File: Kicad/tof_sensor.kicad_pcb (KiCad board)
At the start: 2 copper layers, 86.4 x 45.7 mm, 52 parts, among them J1 Conn_01x06_Male, J2 Conn_01x05, Q1 BSH202,215, SW1 SW_DIP_x03, U1 MIC5504-2.8YM5, U2 PIC24FJ64GA002, U3 VL53L0X, U4 VL53L0X, U5 PCA9306

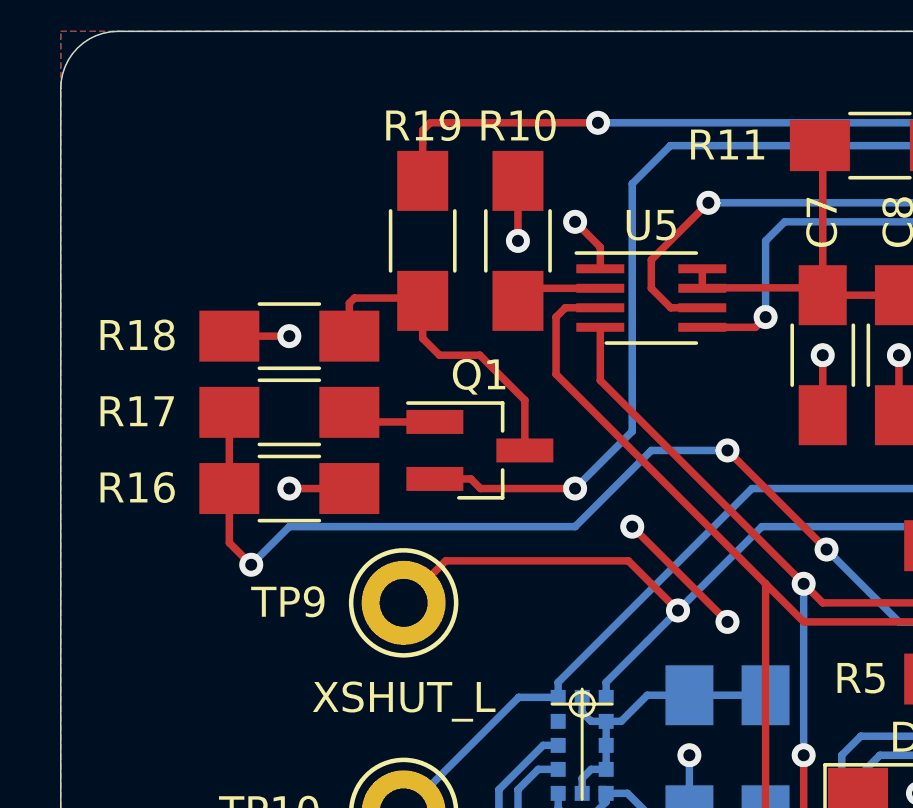
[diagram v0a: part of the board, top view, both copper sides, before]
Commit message: Changed P-MOS by N-MOS for int circuit.
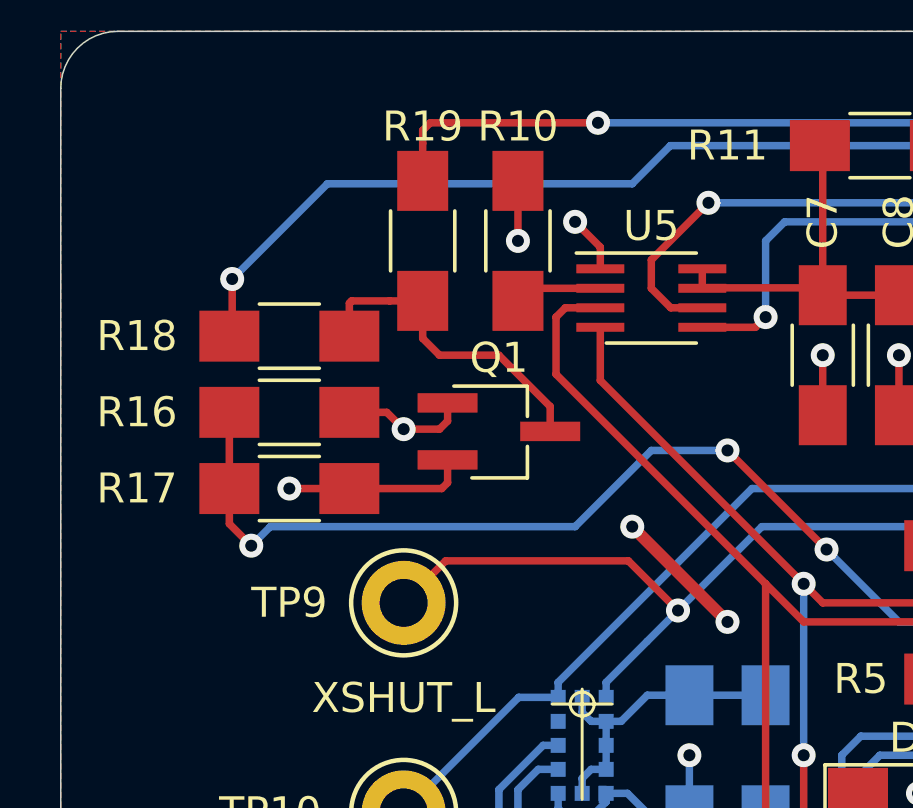
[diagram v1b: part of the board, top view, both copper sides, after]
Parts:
- Q1: value BSH202,215 -> Q_NMOS_SGD; footprint TO_SOT_Packages_SMD:SOT-23_Handsoldering -> TO_SOT_Packages_SMD:TSOT-23_HandSoldering
- moved R16 2.54 mm to (118.7, 73.7)
- moved R17 2.54 mm to (118.7, 76.2)
- moved Q1 0.90 mm to (125.7, 74.3)
- turned R18 to 180 degrees
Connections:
- Q1 pad 1: Net-(Q1-Pad1) -> GND
- Q1 pad 2: VCC -> Net-(Q1-Pad2)
- R17 pad 2: Net-(Q1-Pad1) -> Net-(Q1-Pad2)
- R18 pad 1: GND -> Net-(Q1-Pad3)
- R18 pad 2: Net-(Q1-Pad3) -> VCC
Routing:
- net Net-(Q1-Pad2): track 0.00 -> 6.12 mm, vias 0 -> 1
- net Net-(Q1-Pad1): track 3.62 -> 0.00 mm
- net GND: track 72.4 -> 73.6 mm, vias 23 -> 22
- net /INT_OUT_VDD: track 52.6 -> 51.7 mm
- net VCC: track 85.5 -> 86.4 mm
- net Net-(Q1-Pad3): track 11.4 -> 12.1 mm

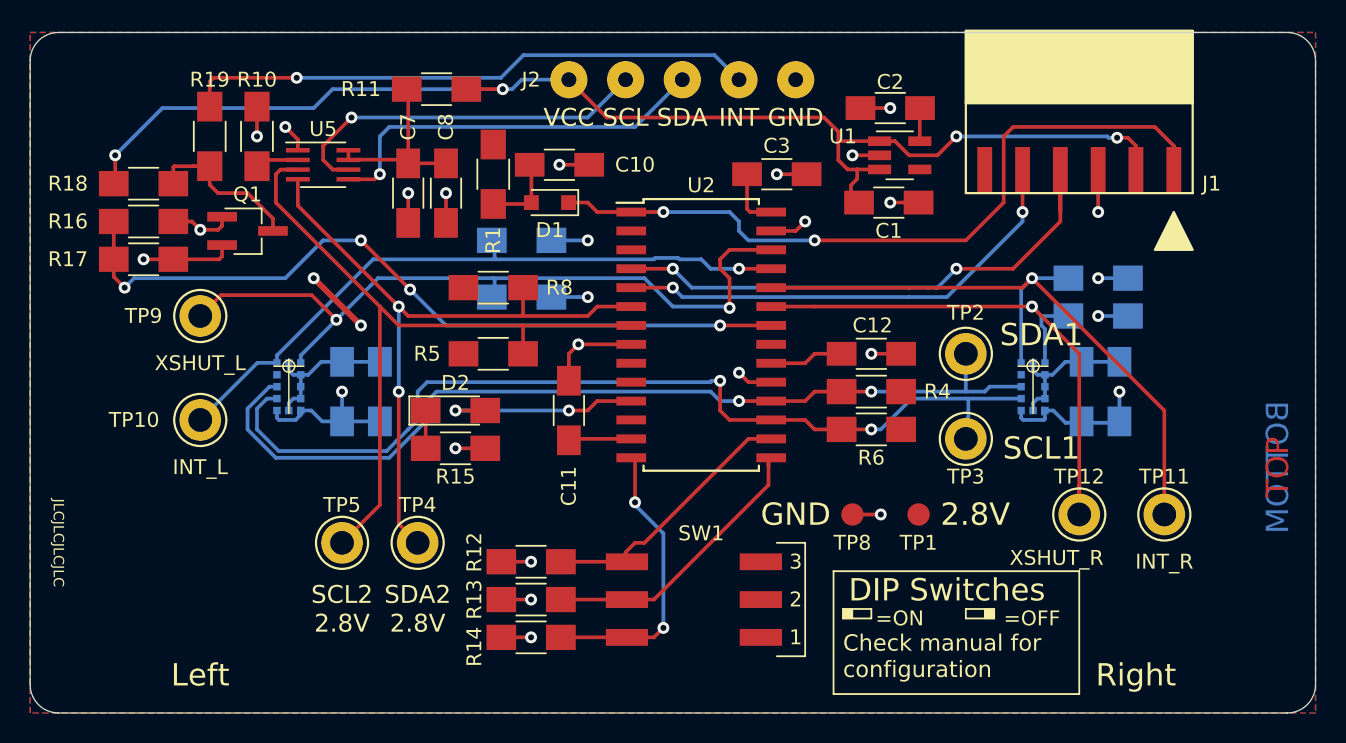
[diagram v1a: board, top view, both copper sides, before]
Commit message: Updated testpoints
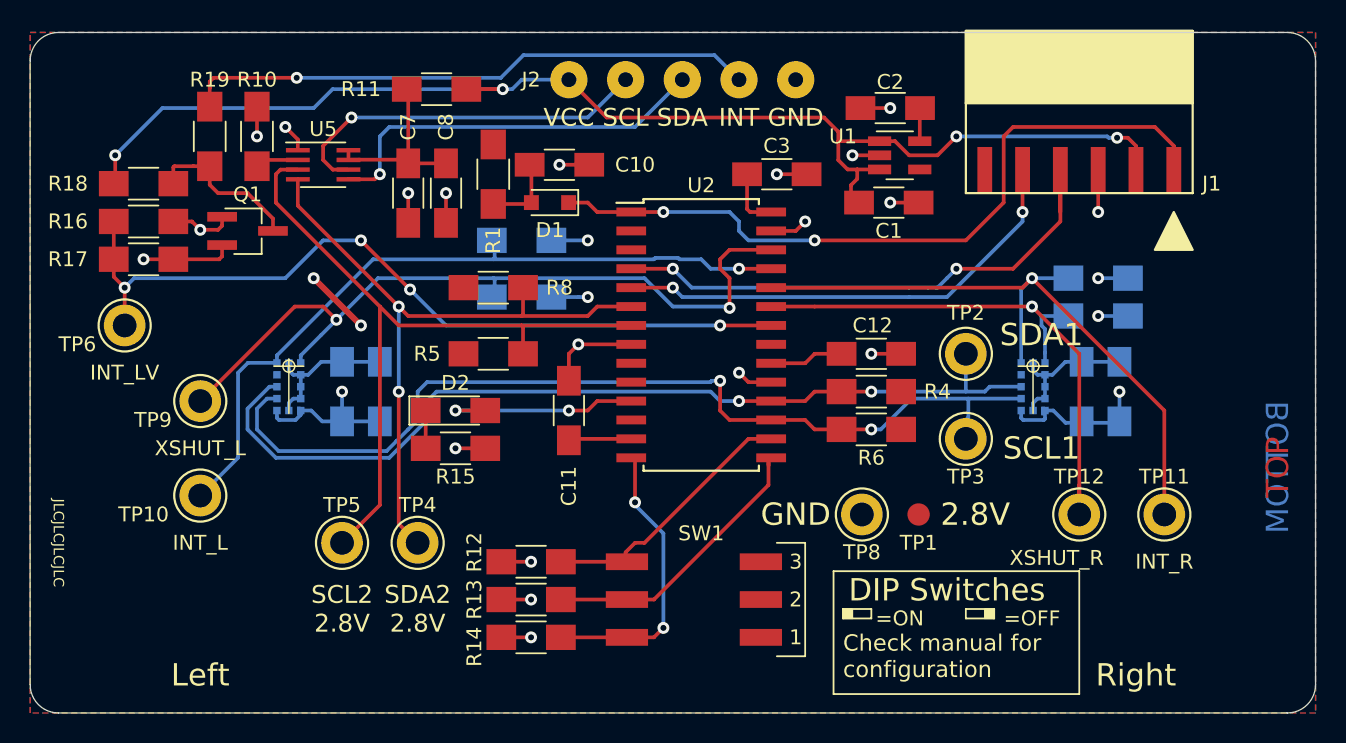
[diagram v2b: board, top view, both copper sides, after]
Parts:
- added TP6: TestPoint_Probe, Measurement_Points:Test_Point_Keystone_5010-5014_Multipurpose, F.Cu at (117.5, 80.6)
- TP8: footprint Measurement_Points:Measurement_Point_Round-SMD-Pad_Small -> Measurement_Points:Test_Point_Keystone_5010-5014_Multipurpose
- moved TP9 5.71 mm to (122.6, 85.7)
- moved TP10 5.08 mm to (122.6, 92.1)
- moved TP8 0.63 mm to (167.0, 93.3)
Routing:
- net /INT_L: track 44.6 -> 50.0 mm
- net /INT_OUT_VDD: track 51.7 -> 54.2 mm
- net GND: track 73.6 -> 71.7 mm, vias 22 -> 21
- net /XSHUT_L: track 51.0 -> 52.8 mm
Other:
- board text added: "INT_LV"
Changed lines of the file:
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@@
   (general
     (thickness 1.6)
-    (drawings 68)
+    (drawings 69)
     (tracks 438)
     (zones 0)
-    (modules 52)
+    (modules 53)
     (nets 39)
   )
@@
     (uvia_drill 0.1)
   )
+  (module Measurement_Points:Test_Point_Keystone_5010-5014_Multipurpose (layer F.Cu)
+    (at 167.005 93.345)
+    (descr "Keystone Miniature THM Test Point 5010-5014, http://www.keyelco.com/product-pdf.cfm?p=1319")
+    (tags "Through Hole Mount Test Points")
+    (attr virtual)
+    (fp_text reference TP8 (at 0 2.54) (layer F.SilkS)
+      (effects (font (size 1 1) (thickness 0.15)))
+    )
+    (fp_text value TestPoint_Probe (at 0 2.75) (layer F.Fab)
+      (effects (font (size 1 1) (thickness 0.15)))
+    )
+    (fp_circle (center 0 0) (end 2 0) (layer F.CrtYd) (width 0.05))
+    (fp_line (start -1.25 -0.4) (end 1.25 -0.4) (layer F.Fab) (width 0.15))
+    (fp_line (start 1.25 -0.4) (end 1.25 0.4) (layer F.Fab) (width 0.15))
+    (fp_line (start 1.25 0.4) (end -1.25 0.4) (layer F.Fab) (width 0.15))
+    (fp_line (start -1.25 0.4) (end -1.25 -0.4) (layer F.Fab) (width 0.15))
+    (fp_circle (center 0 0) (end 1.6 0) (layer F.Fab) (width 0.15))
+    (fp_circle (center 0 0) (end 1.75 0) (layer F.SilkS) (width 0.15))
+    (pad 1 thru_hole circle (at 0 0) (size 2.8 2.8) (drill 1.6) (layers *.Cu *.Mask)
+      (net 2 GND))
+  )
+  (module Measurement_Points:Test_Point_Keystone_5010-5014_Multipurpose (layer F.Cu)
+    (at 117.475 80.645)
+    (descr "Keystone Miniature THM Test Point 5010-5014, http://www.keyelco.com/product-pdf.cfm?p=1319")
+    (tags "Through Hole Mount Test Points")
+    (attr virtual)
+    (fp_text reference TP6 (at -3.175 1.27) (layer F.SilkS)
+      (effects (font (size 1 1) (thickness 0.15)))
+    )
+    (fp_text value TestPoint_Probe (at 0 2.75) (layer F.Fab)
+      (effects (font (size 1 1) (thickness 0.15)))
+    )
+    (fp_circle (center 0 0) (end 2 0) (layer F.CrtYd) (width 0.05))
+    (fp_line (start -1.25 -0.4) (end 1.25 -0.4) (layer F.Fab) (width 0.15))
+    (fp_line (start 1.25 -0.4) (end 1.25 0.4) (layer F.Fab) (width 0.15))
+    (fp_line (start 1.25 0.4) (end -1.25 0.4) (layer F.Fab) (width 0.15))
+    (fp_line (start -1.25 0.4) (end -1.25 -0.4) (layer F.Fab) (width 0.15))
+    (fp_circle (center 0 0) (end 1.6 0) (layer F.Fab) (width 0.15))
+    (fp_circle (center 0 0) (end 1.75 0) (layer F.SilkS) (width 0.15))
+    (pad 1 thru_hole circle (at 0 0) (size 2.8 2.8) (drill 1.6) (layers *.Cu *.Mask)
+      (net 37 /INT_OUT_VDD))
+  )
   (module TO_SOT_Packages_SMD:TSOT-23_HandSoldering (layer F.Cu)
     (at 125.73 74.295)
@@
   )
   (module Measurement_Points:Test_Point_Keystone_5010-5014_Multipurpose (layer F.Cu)
-    (at 122.555 80.01)
+    (at 122.555 85.725)
     (descr "Keystone Miniature THM Test Point 5010-5014, http://www.keyelco.com/product-pdf.cfm?p=1319")
     (tags "Through Hole Mount Test Points")
     (attr virtual)
-    (fp_text reference TP9 (at -3.81 0) (layer F.SilkS)
+    (fp_text reference TP9 (at -3.175 1.27) (layer F.SilkS)
       (effects (font (size 1 1) (thickness 0.15)))
     )
@@
   )
   (module Measurement_Points:Test_Point_Keystone_5010-5014_Multipurpose (layer F.Cu)
-    (at 122.555 86.995)
+    (at 122.555 92.075)
     (descr "Keystone Miniature THM Test Point 5010-5014, http://www.keyelco.com/product-pdf.cfm?p=1319")
     (tags "Through Hole Mount Test Points")
     (attr virtual)
-    (fp_text reference TP10 (at -4.445 0) (layer F.SilkS)
+    (fp_text reference TP10 (at -3.81 1.27) (layer F.SilkS)
       (effects (font (size 1 1) (thickness 0.15)))
     )
@@
       (rotate (xyz 0 0 0))
     )
-  )
-  (module Measurement_Points:Measurement_Point_Round-SMD-Pad_Small (layer F.Cu)
-    (at 166.37 93.345)
-    (descr "Mesurement Point, Round, SMD Pad, DM 1.5mm,")
-    (tags "Mesurement Point Round SMD Pad 1.5mm")
-    (attr virtual)
-    (fp_text reference TP8 (at 0 1.905) (layer F.SilkS)
-      (effects (font (size 1 1) (thickness 0.15)))
-    )
-    (fp_text value TestPoint_Probe (at 0 2) (layer F.Fab)
-      (effects (font (size 1 1) (thickness 0.15)))
-    )
-    (fp_circle (center 0 0) (end 1 0) (layer F.CrtYd) (width 0.05))
-    (pad 1 smd circle (at 0 0) (size 1.5 1.5) (layers F.Cu F.Mask)
-      (net 2 GND))
   )
   (module Measurement_Points:Measurement_Point_Round-SMD-Pad_Small (layer F.Cu)
@@
     )
   )
-  (gr_text INT_L (at 122.555 90.17) (layer F.SilkS)
+  (gr_text INT_LV (at 117.475 83.82) (layer F.SilkS)
+    (effects (font (size 1 1) (thickness 0.25)))
+  )
+  (gr_text INT_L (at 122.555 95.25) (layer F.SilkS)
     (effects (font (size 1 1) (thickness 0.25)))
   )
@@
     (effects (font (size 1.5 1.5) (thickness 0.3)))
   )
-  (gr_text XSHUT_L (at 122.555 83.185) (layer F.SilkS)
+  (gr_text XSHUT_L (at 122.555 88.9) (layer F.SilkS)
     (effects (font (size 1 1) (thickness 0.25)))
   )
@@
   (segment (start 148.685 69.85) (end 146.685 69.85) (width 0.25) (layer F.Cu) (net 2) (status 10))
   (via (at 146.685 69.85) (size 0.8) (drill 0.4) (layers F.Cu B.Cu) (net 2))
-  (segment (start 166.37 93.345) (end 168.275 93.345) (width 0.25) (layer F.Cu) (net 2) (status 10))
-  (via (at 168.275 93.345) (size 0.8) (drill 0.4) (layers F.Cu B.Cu) (net 2))
   (via (at 139.7 88.9) (size 0.8) (drill 0.4) (layers F.Cu B.Cu) (net 2))
   (segment (start 141.7 88.9) (end 139.7 88.9) (width 0.25) (layer F.Cu) (net 2) (status 10))
@@
   (segment (start 142.24 76.2) (end 142.335 76.105) (width 0.25) (layer B.Cu) (net 13))
   (segment (start 134.165 76.2) (end 142.24 76.2) (width 0.25) (layer B.Cu) (net 13))
-  (segment (start 126.39 83.16) (end 127.705 83.16) (width 0.25) (layer B.Cu) (net 13))
-  (segment (start 122.555 86.995) (end 126.39 83.16) (width 0.25) (layer B.Cu) (net 13))
   (segment (start 129.305 83.16) (end 129.305 82.66) (width 0.25) (layer B.Cu) (net 14) (status 10))
   (via (at 158.115 79.465) (size 0.8) (drill 0.4) (layers F.Cu B.Cu) (net 14))
@@
   (segment (start 134.495 77.47) (end 142.24 77.47) (width 0.25) (layer B.Cu) (net 14))
   (via (at 131.7 80.265) (size 0.8) (drill 0.4) (layers F.Cu B.Cu) (net 14))
-  (segment (start 130.81 79.375) (end 131.7 80.265) (width 0.25) (layer F.Cu) (net 14))
   (segment (start 134.495 77.47) (end 131.7 80.265) (width 0.25) (layer B.Cu) (net 14))
   (segment (start 131.7 80.265) (end 130.6675 81.2975) (width 0.25) (layer B.Cu) (net 14))
-  (segment (start 130.045001 78.610001) (end 130.81 79.375) (width 0.25) (layer F.Cu) (net 14))
-  (segment (start 123.954999 78.610001) (end 130.045001 78.610001) (width 0.25) (layer F.Cu) (net 14))
-  (segment (start 122.555 80.01) (end 123.954999 78.610001) (width 0.25) (layer F.Cu) (net 14))
   (segment (start 142.24 77.47) (end 152.4 77.47) (width 0.25) (layer B.Cu) (net 14))
   (segment (start 158.025 79.375) (end 154.305 79.375) (width 0.25) (layer B.Cu) (net 14))
@@
   (segment (start 124.02 73.95) (end 124.02 73.345) (width 0.25) (layer F.Cu) (net 2))
   (segment (start 123.75 74.22) (end 124.02 73.95) (width 0.25) (layer F.Cu) (net 2))
+  (segment (start 125.095 89.535) (end 122.555 92.075) (width 0.25) (layer B.Cu) (net 13))
+  (segment (start 125.095 83.82) (end 125.095 89.535) (width 0.25) (layer B.Cu) (net 13))
+  (segment (start 127.705 83.16) (end 125.755 83.16) (width 0.25) (layer B.Cu) (net 13))
+  (segment (start 125.755 83.16) (end 125.095 83.82) (width 0.25) (layer B.Cu) (net 13))
+  (segment (start 131.7 80.265) (end 130.81 79.375) (width 0.25) (layer F.Cu) (net 14))
+  (segment (start 128.905 79.375) (end 122.555 85.725) (width 0.25) (layer F.Cu) (net 14))
+  (segment (start 130.81 79.375) (end 128.905 79.375) (width 0.25) (layer F.Cu) (net 14))
   (segment (start 123.19 69.945) (end 122.65 69.945) (width 0.25) (layer F.Cu) (net 36))
   (segment (start 122.65 69.945) (end 122.555 69.85) (width 0.25) (layer F.Cu) (net 36))
@@
   (segment (start 116.745 77.375) (end 116.745 76.2) (width 0.25) (layer F.Cu) (net 37))
   (segment (start 117.475 78.105) (end 116.745 77.375) (width 0.25) (layer F.Cu) (net 37))
+  (segment (start 117.475 78.105) (end 117.475 80.645) (width 0.25) (layer F.Cu) (net 37))
   (segment (start 124.02 76.005) (end 124.02 75.245) (width 0.25) (layer F.Cu) (net 38))
   (segment (start 120.745 76.2) (end 123.825 76.2) (width 0.25) (layer F.Cu) (net 38))

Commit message: Replaced mounting holes that went missing
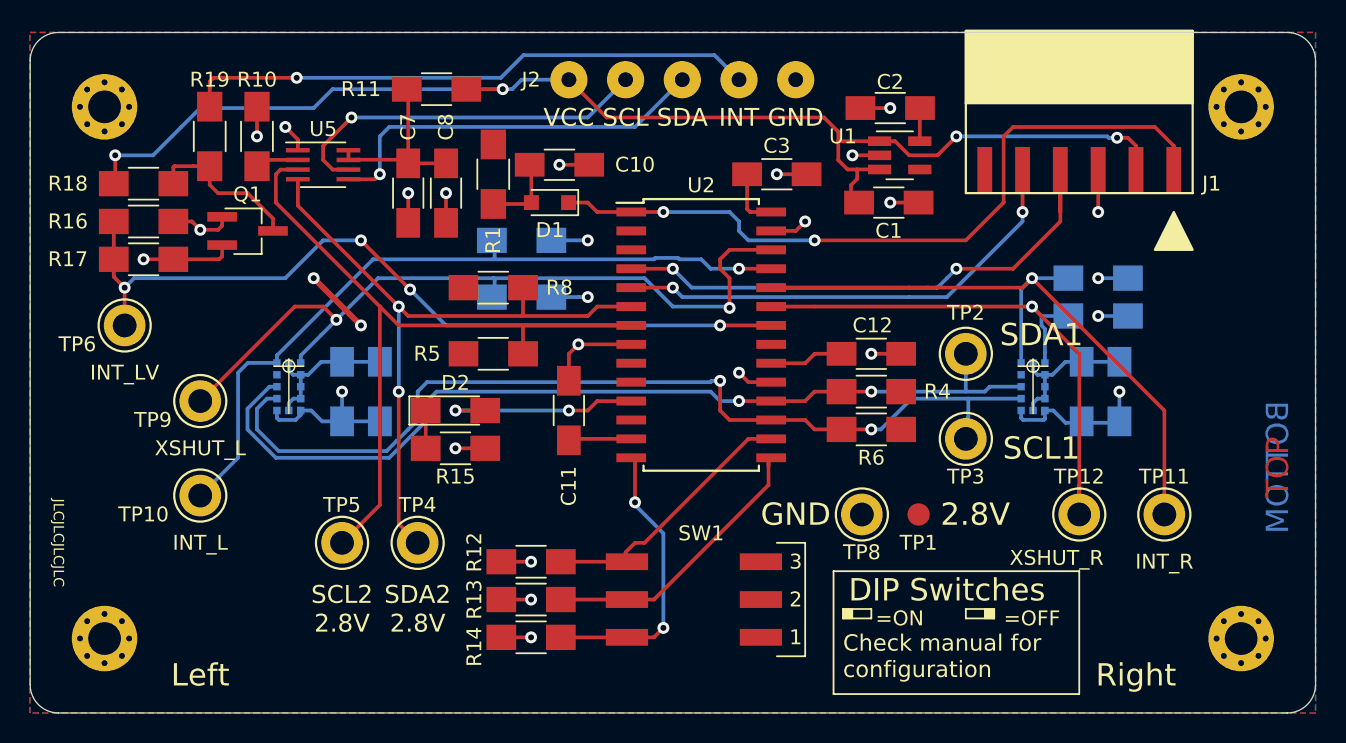
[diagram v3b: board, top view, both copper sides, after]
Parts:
- added REF**: MountingHole_2.2mm_M2_Pad_Via, Mounting_Holes:MountingHole_2.2mm_M2_Pad_Via, F.Cu at (116.1, 66.0)
- added REF**: MountingHole_2.2mm_M2_Pad_Via, Mounting_Holes:MountingHole_2.2mm_M2_Pad_Via, F.Cu at (192.5, 66.0)
- added REF**: MountingHole_2.2mm_M2_Pad_Via, Mounting_Holes:MountingHole_2.2mm_M2_Pad_Via, F.Cu at (116.1, 101.7)
- added REF**: MountingHole_2.2mm_M2_Pad_Via, Mounting_Holes:MountingHole_2.2mm_M2_Pad_Via, F.Cu at (192.5, 101.7)

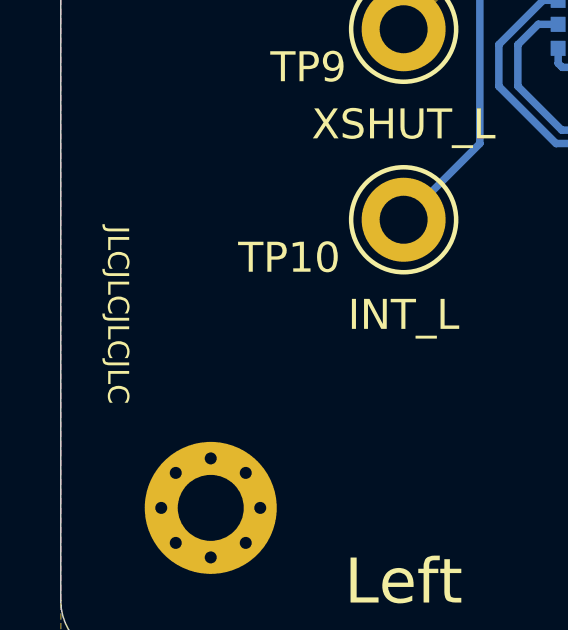
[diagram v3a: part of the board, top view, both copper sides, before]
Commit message: Removed JLCJLCJLCJLC text label
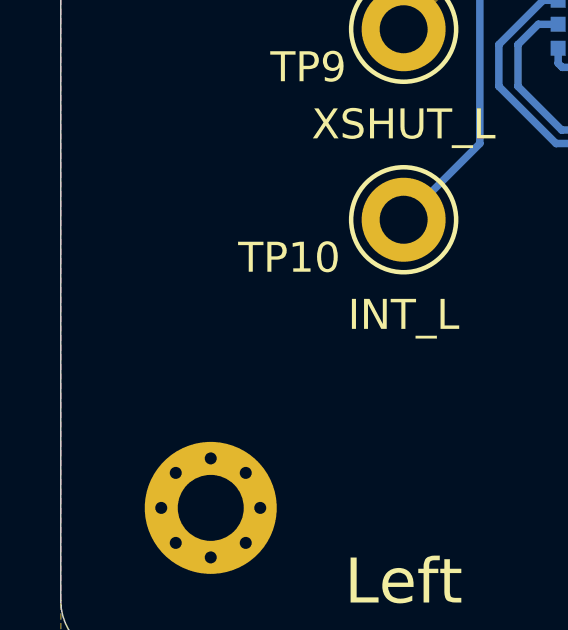
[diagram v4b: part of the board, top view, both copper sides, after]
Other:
- board text removed: "JLCJLCJLCJLC"
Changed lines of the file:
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@@
   (general
     (thickness 1.6)
-    (drawings 69)
+    (drawings 68)
     (tracks 440)
     (zones 0)
@@
   (gr_line (start 165.1 105.41) (end 165.1 97.155) (layer F.SilkS) (width 0.12))
   (gr_line (start 181.61 105.41) (end 165.1 105.41) (layer F.SilkS) (width 0.12))
-  (gr_text JLCJLCJLCJLC (at 113.03 95.25 270) (layer F.SilkS)
-    (effects (font (size 0.7 0.7) (thickness 0.15)))
-  )
   (gr_line (start 163.195 102.87) (end 161.29 102.87) (layer F.SilkS) (width 0.12))
   (gr_line (start 163.195 95.25) (end 163.195 102.87) (layer F.SilkS) (width 0.12))
